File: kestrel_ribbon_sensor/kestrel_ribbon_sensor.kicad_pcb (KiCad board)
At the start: 6 copper layers, 48 x 48 mm, 26 parts, among them J1 SHF-120-01-L-D-SM, J2 SHF-120-01-L-D-SM, J3 DEBUG_HEADER

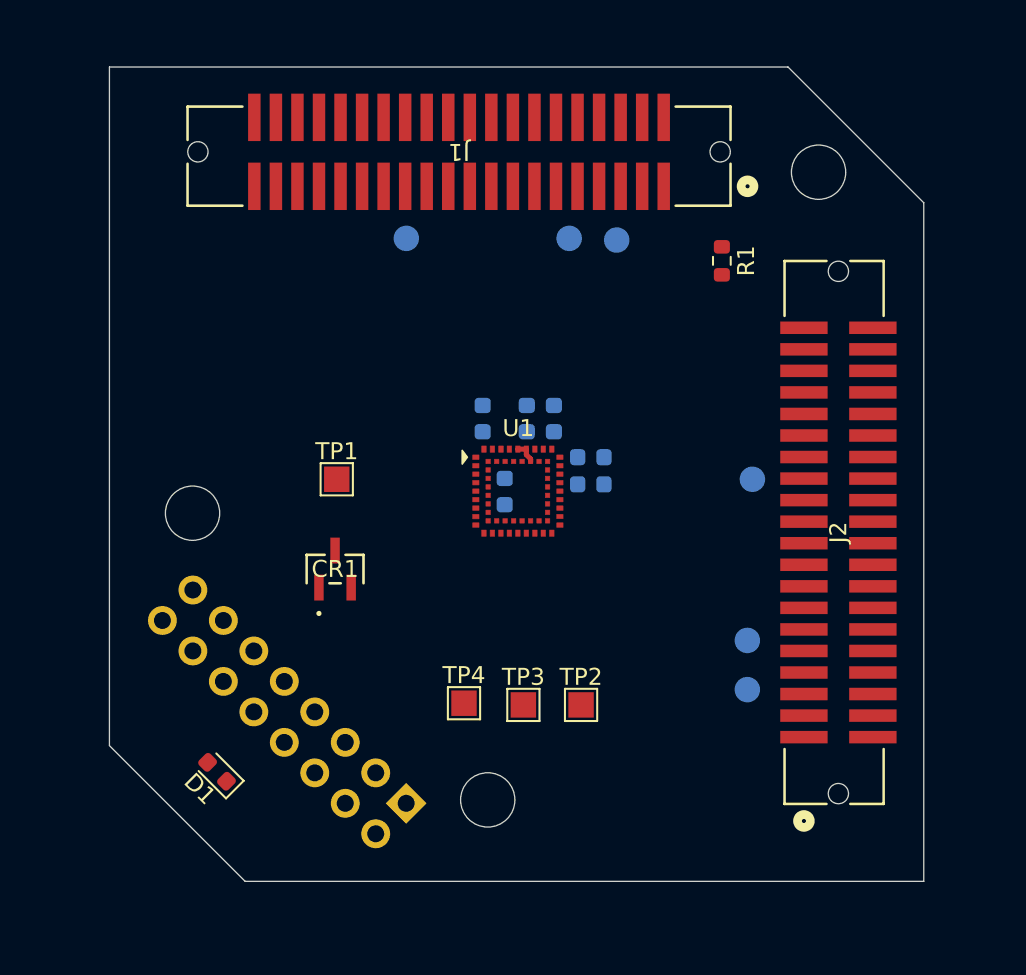
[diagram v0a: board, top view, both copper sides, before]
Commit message: beginning routing for sensor pcb
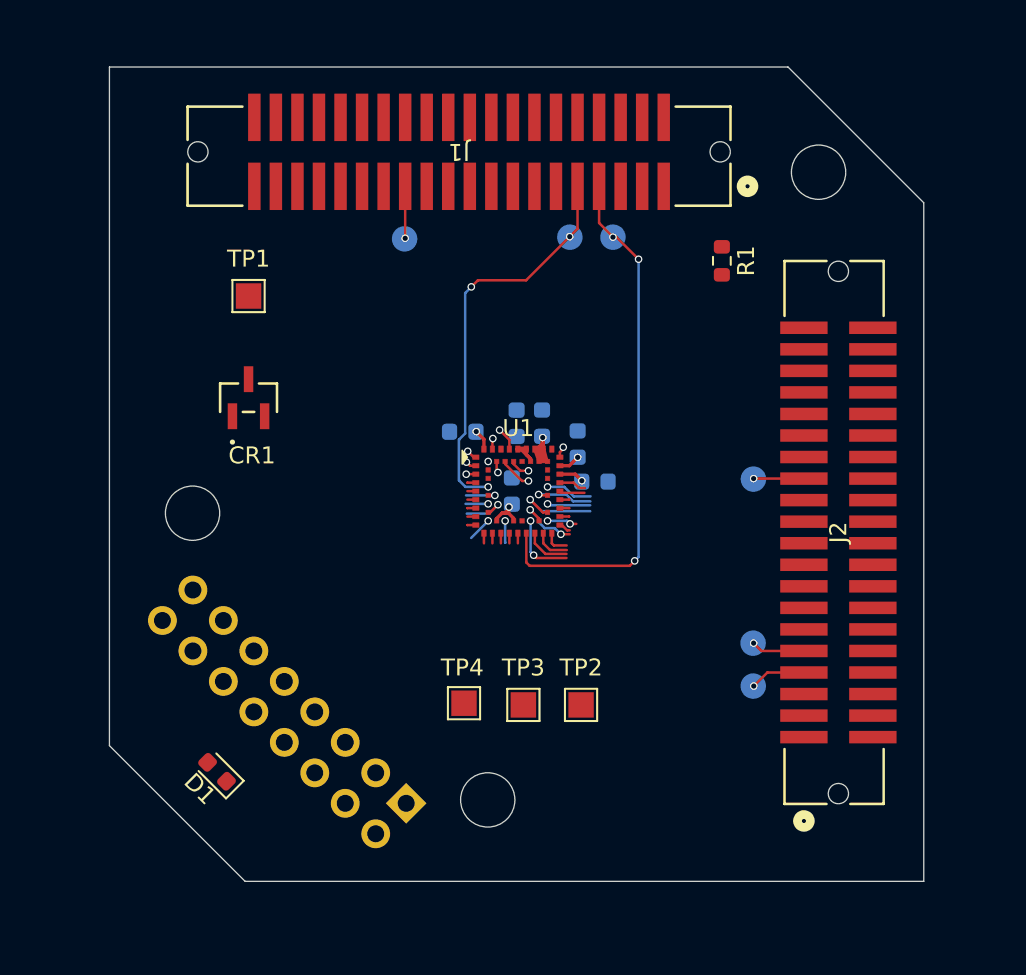
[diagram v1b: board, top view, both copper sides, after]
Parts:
- moved TP1 12.0 mm to (147.7, 71.0)
- moved CR1 11.3 mm to (147.7, 77.0)
- moved C4 1.41 mm to (160.3, 79.0), turned to 180 degrees
- moved C3 1.10 mm to (167.1, 79.7), turned to -90 degrees
- moved C2 0.75 mm to (165.0, 78.5)
- moved C5 0.66 mm to (163.5, 78.5)
- moved C6 0.42 mm to (163.2, 82.5)
- moved TP6 0.41 mm to (177.4, 94.0)
- moved TP8 0.38 mm to (177.4, 91.5)
- moved C1 0.29 mm to (168.1, 81.9)
- moved TP5 0.28 mm to (169.2, 67.5)
- moved TP9 0.10 mm to (156.9, 67.6)
- moved TP7 0.08 mm to (166.6, 67.5)
- moved TP10 0.06 mm to (177.5, 81.8)
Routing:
- net /CLK_IO: track 0.00 -> 31.6 mm, vias 0 -> 3
- net /D1_0: track 0.00 -> 23.8 mm, vias 0 -> 3
- net /D4_0: track 0.00 -> 8.14 mm, vias 0 -> 2
- net /D3_0: track 0.00 -> 7.35 mm, vias 0 -> 3
- net /D3_2: track 0.00 -> 3.93 mm, vias 0 -> 2
- net /V3V3: track 0.00 -> 3.91 mm, vias 0 -> 1
- net /DATAVAL: track 0.00 -> 3.78 mm, vias 0 -> 1
- net /D4_4: track 0.00 -> 3.76 mm, vias 0 -> 1
- net /D2_0: track 0.00 -> 3.56 mm, vias 0 -> 1
- net /VDDHSIO: track 0.00 -> 3.00 mm, vias 0 -> 1
- net /D1_6: track 0.00 -> 2.81 mm, vias 0 -> 1
- net /D4_6: track 0.00 -> 2.77 mm, vias 0 -> 1
- net /D3_1: track 0.00 -> 2.72 mm
- net /D4_2: track 0.00 -> 2.55 mm, vias 0 -> 1
- net /V1V8: track 1.33 -> 3.56 mm, vias 0 -> 1
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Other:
- copper layers 6 -> 4

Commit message: finish routing for sensor->ribbon pcb
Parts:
- TP3: footprint TestPoint:TestPoint_Pad_1.5x1.5mm -> TestPoint:TestPoint_Pad_D1.0mm; moved to B.Cu
- moved TP4 12.1 mm to (150.5, 88.0), turned to 45 degrees
- moved TP2 10.1 mm to (174.6, 102.1)
- moved TP3 9.81 mm to (163.6, 85.3), turned to 180 degrees
- moved CR1 6.51 mm to (145.4, 70.9)
- moved TP1 6.32 mm to (145.4, 76.9)
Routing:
- net /V3V3: track 3.91 -> 68.3 mm, vias 1 -> 2
- net /SPI_CS: track 0.62 -> 56.5 mm, vias 1 -> 5
- net /SPI_MISO: track 0.00 -> 51.2 mm, vias 1 -> 2
- net /GPIO2: track 1.94 -> 52.3 mm, vias 1 -> 2
- net /ENABLE: track 0.63 -> 50.8 mm, vias 1 -> 3
- net /SPI_CLK: track 0.57 -> 49.9 mm, vias 1 -> 3
- net /SPI_MOSI: track 0.64 -> 48.2 mm, vias 1 -> 2
- net /GPIO4: track 1.19 -> 48.4 mm, vias 1 -> 3
- net /GPIO1: track 0.68 -> 47.4 mm, vias 1 -> 2
- net /GPIO3: track 1.36 -> 47.9 mm, vias 1 -> 2
- net /D2_7: track 0.60 -> 38.9 mm
- net /D2_6: track 0.60 -> 38.8 mm
- net /D2_4: track 0.60 -> 38.7 mm
- net /D2_2: track 0.60 -> 38.7 mm
- net /D2_3: track 0.60 -> 38.7 mm
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- added copper zone on B.Cu, net GND
- added copper zone on F.Cu, net GND
- added copper zone on In1.Cu, net GND
- added copper zone on In2.Cu, net GND

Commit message: sensor gerber
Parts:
- renumbered TP4 to 1v8, TP2 to 3v3, TP5 to CLK, TP7 to D1, TP9 to D2, TP8 to D3, TP10 to D4, TP1 to N1v5, TP6 to VAL, TP3 to VHIO
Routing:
- net /GPIO2: track 52.3 -> 53.3 mm
- net /VDDHSIO: track 5.11 -> 4.40 mm
